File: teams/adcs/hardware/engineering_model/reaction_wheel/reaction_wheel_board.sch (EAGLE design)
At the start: 93 parts, among them U2 TPS732XX, U3 TPS732XX

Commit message: ADCS/RW: Include new SEPIC layout
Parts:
- added C8: 10 uF, rcl:C-USC0805
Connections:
- net N$1 renamed VD
- net GND: now also C8.2, U$2.WHEEL_GND@71, U$2.WHEEL_GND@72; no longer U$2.BDOT_3.3V@84, U$2.BDOT_5V@82
- net VBAT: now also C8.1, U$2.WHEEL_VBATT@69, U$2.WHEEL_VBATT@70; no longer U$2.BDOT_3.3V@83, U$2.BDOT_5V@81
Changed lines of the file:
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@@
 <?xml version="1.0" encoding="utf-8"?>
 <!DOCTYPE eagle SYSTEM "eagle.dtd">
-<eagle version="8.4.1">
+<eagle version="8.4.3">
 <drawing>
 <settings>
@@
 <part name="MOTOR_Y_DEBUG" library="SparkFun-Connectors" deviceset="CONN_03" device="LOCK"/>
 <part name="MOTOR_Z_DEBUG" library="SparkFun-Connectors" deviceset="CONN_03" device="LOCK"/>
+<part name="GND56" library="supply1" library_urn="urn:adsk.eagle:library:371" deviceset="GND" device=""/>
+<part name="C8" library="rcl" library_urn="urn:adsk.eagle:library:334" deviceset="C-US" device="C0805" package3d_urn="urn:adsk.eagle:package:23617/2" value="10 uF"/>
 </parts>
 <sheets>
@@
 <instance part="U$3" gate="G$1" x="0" y="-78.74"/>
 <instance part="U$4" gate="G$1" x="63.5" y="-129.54" rot="R270"/>
-<instance part="GND1" gate="1" x="20.32" y="25.4" rot="R90"/>
-<instance part="GND2" gate="1" x="96.52" y="25.4" rot="R90"/>
+<instance part="GND1" gate="1" x="33.02" y="33.02" rot="R270"/>
+<instance part="GND2" gate="1" x="93.98" y="33.02" rot="R90"/>
 <instance part="GND3" gate="1" x="71.12" y="-104.14" rot="R180"/>
 <instance part="GND4" gate="1" x="-48.26" y="-60.96" rot="R270"/>
@@
 <instance part="MOTOR_Y_DEBUG" gate="J$1" x="228.6" y="-58.42" rot="R180"/>
 <instance part="MOTOR_Z_DEBUG" gate="J$1" x="381" y="-58.42" rot="R180"/>
+<instance part="GND56" gate="1" x="-78.74" y="22.86"/>
+<instance part="C8" gate="G$1" x="-78.74" y="33.02"/>
 </instances>
 <busses>
@@
 <net name="GND" class="0">
 <segment>
-<pinref part="U$2" gate="G$1" pin="BDOT_5V@82"/>
-<pinref part="GND1" gate="1" pin="GND"/>
-<wire x1="12.7" y1="25.4" x2="17.78" y2="25.4" width="0.1524" layer="91"/>
-</segment>
-<segment>
-<pinref part="GND2" gate="1" pin="GND"/>
-<pinref part="U$2" gate="G$1" pin="BDOT_3.3V@84"/>
-<wire x1="93.98" y1="25.4" x2="88.9" y2="25.4" width="0.1524" layer="91"/>
-</segment>
-<segment>
 <pinref part="U$4" gate="G$1" pin="GND@2"/>
 <pinref part="GND3" gate="1" pin="GND"/>
@@
 <label x="368.3" y="-53.34" size="1.778" layer="95" rot="R180" xref="yes"/>
 </segment>
+<segment>
+<pinref part="U$2" gate="G$1" pin="WHEEL_GND@71"/>
+<pinref part="GND1" gate="1" pin="GND"/>
+<wire x1="35.56" y1="33.02" x2="38.1" y2="33.02" width="0.1524" layer="91"/>
+</segment>
+<segment>
+<pinref part="U$2" gate="G$1" pin="WHEEL_GND@72"/>
+<pinref part="GND2" gate="1" pin="GND"/>
+<wire x1="91.44" y1="33.02" x2="88.9" y2="33.02" width="0.1524" layer="91"/>
+</segment>
+<segment>
+<pinref part="GND56" gate="1" pin="GND"/>
+<pinref part="C8" gate="G$1" pin="2"/>
+<wire x1="-78.74" y1="25.4" x2="-78.74" y2="27.94" width="0.1524" layer="91"/>
+</segment>
 </net>
 <net name="CANH" class="0">
@@
 <net name="VBAT" class="0">
 <segment>
-<pinref part="U$2" gate="G$1" pin="BDOT_5V@81"/>
-<wire x1="-40.64" y1="25.4" x2="-45.72" y2="25.4" width="0.1524" layer="91"/>
-<label x="-45.72" y="25.4" size="1.778" layer="95" rot="R180" xref="yes"/>
-</segment>
-<segment>
-<pinref part="U$2" gate="G$1" pin="BDOT_3.3V@83"/>
-<wire x1="38.1" y1="25.4" x2="33.02" y2="25.4" width="0.1524" layer="91"/>
-<label x="33.02" y="25.4" size="1.778" layer="95" rot="R180" xref="yes"/>
+<label x="-50.8" y="30.48" size="1.778" layer="95" rot="R180" xref="yes"/>
+<wire x1="-45.72" y1="30.48" x2="-50.8" y2="30.48" width="0.1524" layer="91"/>
+<wire x1="-45.72" y1="30.48" x2="-45.72" y2="33.02" width="0.1524" layer="91"/>
+<pinref part="U$2" gate="G$1" pin="WHEEL_VBATT@69"/>
+<wire x1="-45.72" y1="33.02" x2="-40.64" y2="33.02" width="0.1524" layer="91"/>
 </segment>
 <segment>
@@
 <wire x1="187.96" y1="25.4" x2="187.96" y2="30.48" width="0.1524" layer="91"/>
 <junction x="187.96" y="25.4"/>
+</segment>
+<segment>
+<pinref part="U$2" gate="G$1" pin="WHEEL_VBATT@70"/>
+<wire x1="12.7" y1="33.02" x2="17.78" y2="33.02" width="0.1524" layer="91"/>
+<label x="17.78" y="33.02" size="1.778" layer="95" xref="yes"/>
+</segment>
+<segment>
+<pinref part="C8" gate="G$1" pin="1"/>
+<wire x1="-78.74" y1="35.56" x2="-78.74" y2="38.1" width="0.1524" layer="91"/>
+<label x="-78.74" y="38.1" size="1.778" layer="95" rot="R90" xref="yes"/>
 </segment>
 </net>
@@
 </segment>
 </net>
-<net name="N$1" class="0">
+<net name="VD" class="0">
 <segment>
 <pinref part="C25" gate="G$1" pin="2"/>

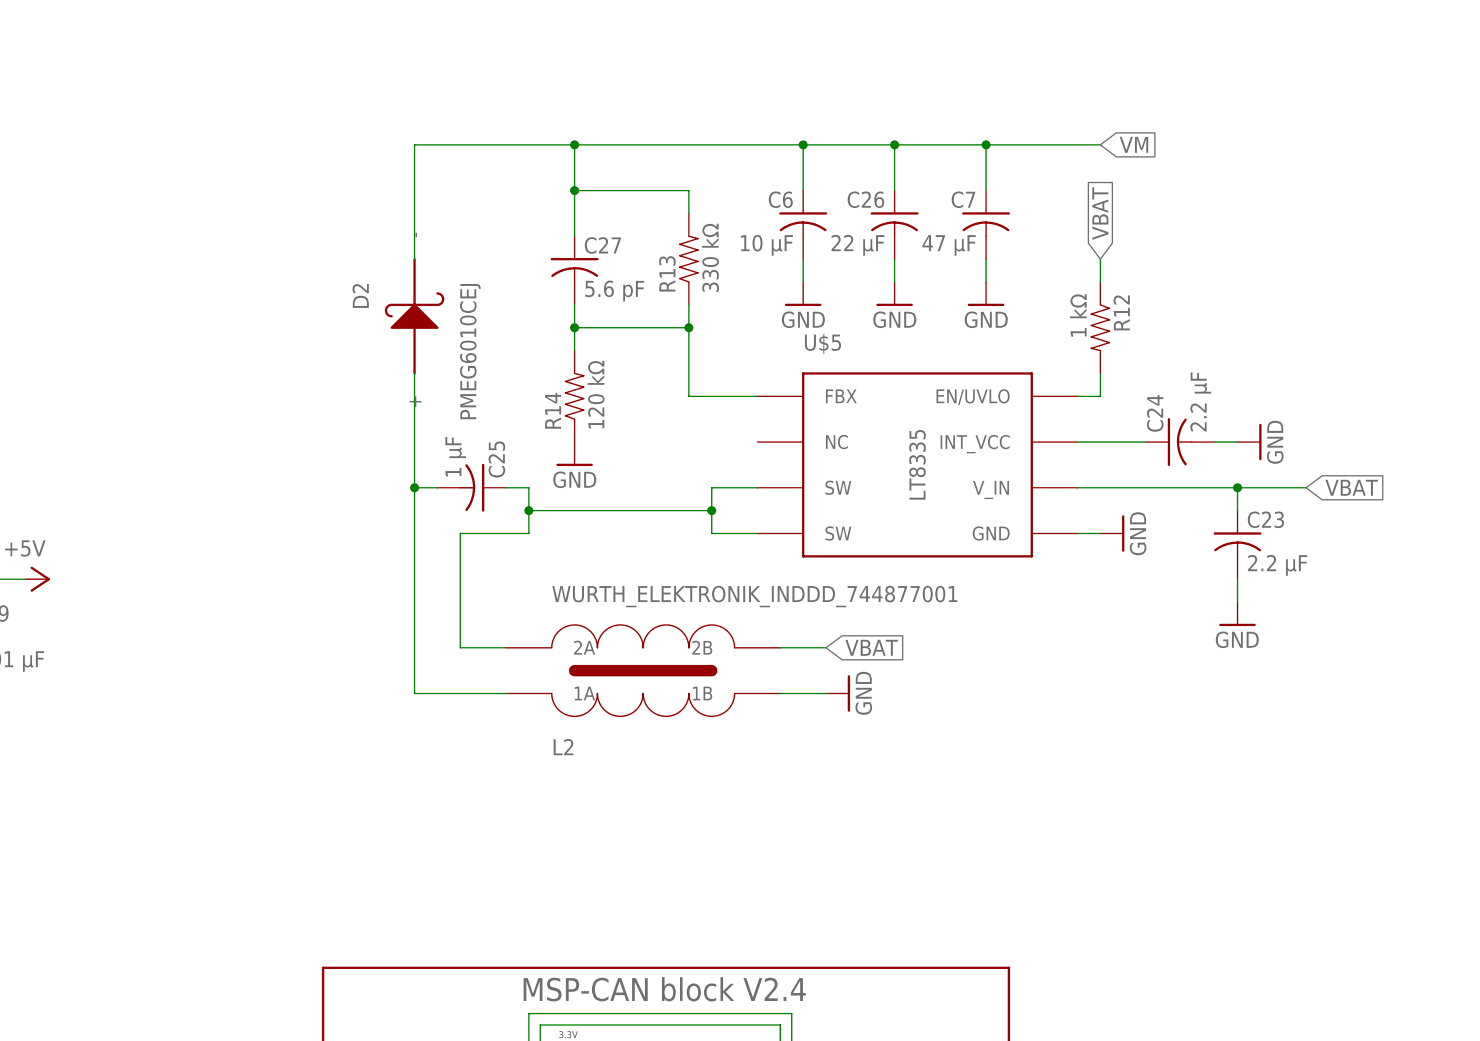
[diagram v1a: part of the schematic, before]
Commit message: ADCS: Switch to new SEPIC layout
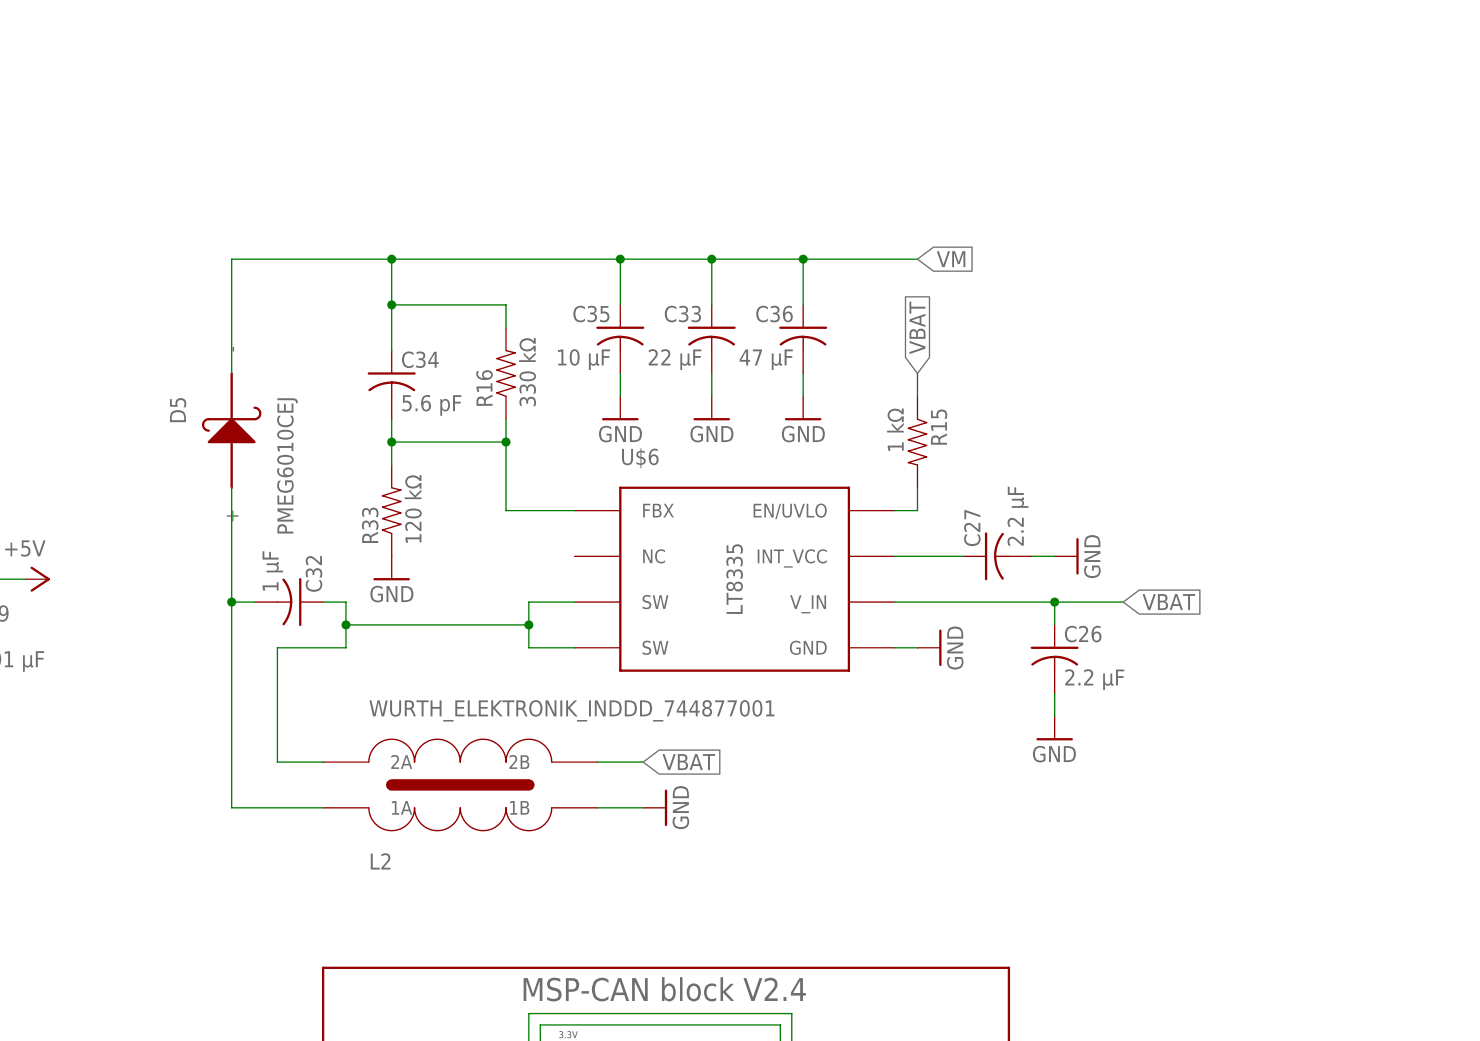
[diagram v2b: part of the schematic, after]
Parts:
- removed C23, C24: 2.2 μF, rcl:C-USC0805
- removed C25: 1 μF, rcl:C-USC0805
- removed C6: 10 μF, rcl:C-USC0805
- removed C7: 47 μF, rcl:C-USC1206
- removed D2: PMEG6010CEJ, DubSat1 Components:PMEG6010CEJ
- removed R12: 1 kΩ, DubSat1 Components:RESISTOR0805
- removed R13: 330 kΩ, DubSat1 Components:RESISTOR0805
- removed R14: 120 kΩ, DubSat1 Components:RESISTOR0805
- removed U$5: LT8335, DubSat1 Components:LT8335
- added C32: 1 μF, rcl:C-USC0805
- added C33: 22 μF, rcl:C-USC1206
- added C34: 5.6 pF, rcl:C-USC0805
- added C35: 10 μF, rcl:C-USC0805
- added C36: 47 μF, rcl:C-USC1206
- added D5: PMEG6010CEJ, DubSat1 Components:PMEG6010CEJ
- added R15: 1 kΩ, DubSat1 Components:RESISTOR0805
- added R16: 330 kΩ, DubSat1 Components:RESISTOR0805
- added R33: 120 kΩ, DubSat1 Components:RESISTOR0805
- added U$6: LT8335, DubSat1 Components:LT8335
- C26: value 22 μF -> 2.2 μF; device rcl:C-USC1206 -> rcl:C-USC0805
- C27: value 5.6 pF -> 2.2 μF
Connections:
- net EN_UVLO: now also R15.2, U$6.EN/UVLO; no longer R12.2, U$5.EN/UVLO
- net FBX: now also C34.2, R16.1, R33.2, U$6.FBX; no longer C27.2, R13.1, R14.2, U$5.FBX
- net GND: now also C27.2, C33.2, C35.2, C36.2, R33.1, U$6.GND; no longer C23.2, C24.2, C6.2, C7.2, R14.1, U$5.GND
- net INT_VCC: now also C27.1, U$6.INT_VCC; no longer C24.1, U$5.INT_VCC
- net SW: now also C32.1, U$6.SW@1, U$6.SW@2; no longer C25.1, U$5.SW@1, U$5.SW@2
- net VBAT: now also C26.1, R15.1, U$6.V_IN; no longer C23.1, R12.1, U$5.V_IN
- net VD: now also C32.2, D5.+; no longer C25.2, D2.+
- net VM: now also C33.1, C34.1, C35.1, C36.1, D5.-, R16.2; no longer C26.1, C27.1, C6.1, C7.1, D2.-, R13.2
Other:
- moved on the sheet: C26, C27, L2

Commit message: ADCS/RW: Update some net and component names
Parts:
- renumbered U$11 to MSP_Y_DEBUG, U$14 to MSP_Z_DEBUG, U$2 to PC104, U$4 to MSP_X_DEBUG

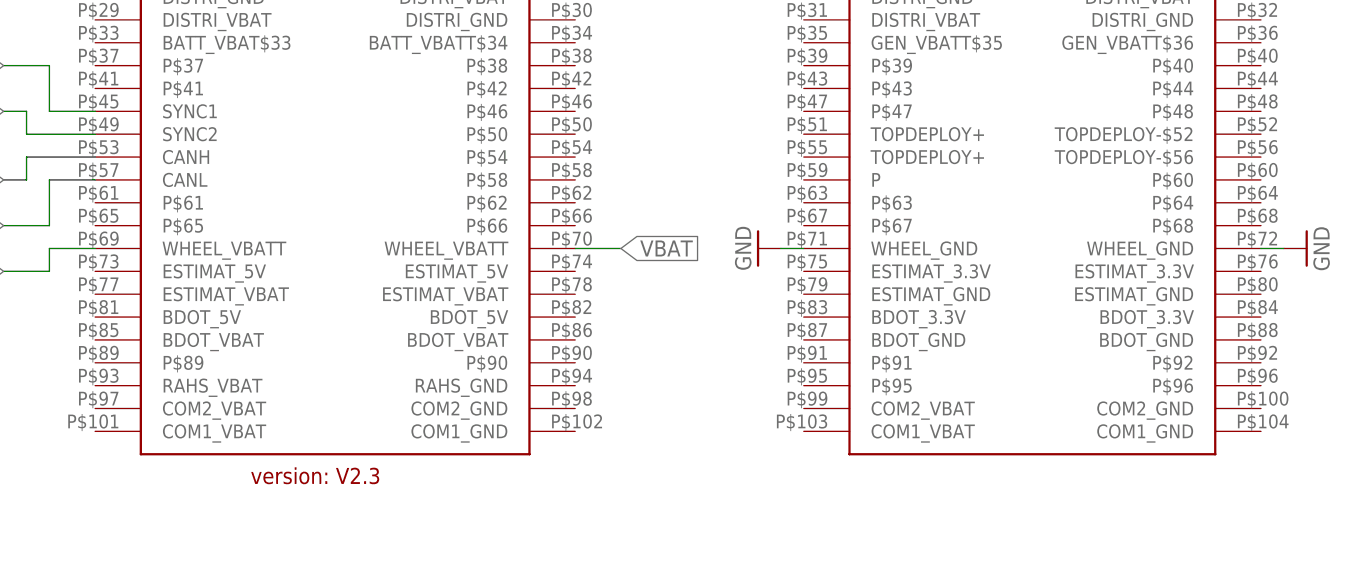
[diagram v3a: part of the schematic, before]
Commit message: ADCS/RW: Move debug LED out from under Picolock connector 😞
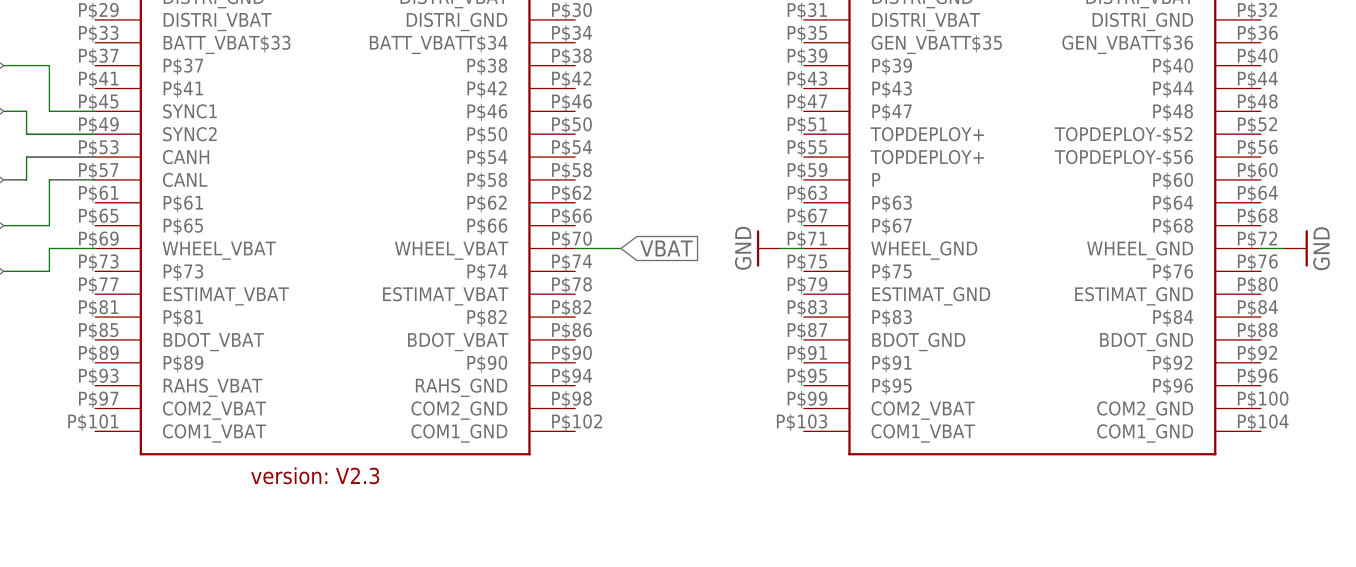
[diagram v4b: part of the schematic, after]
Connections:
- net VBAT: now also PC104.WHEEL_VBAT@69, PC104.WHEEL_VBAT@70; no longer PC104.WHEEL_VBATT@69, PC104.WHEEL_VBATT@70
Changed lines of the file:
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@@
 <?xml version="1.0" encoding="utf-8"?>
 <!DOCTYPE eagle SYSTEM "eagle.dtd">
-<eagle version="8.5.1">
+<eagle version="8.5.0">
 <drawing>
 <settings>
@@
 <wire x1="-45.72" y1="30.48" x2="-50.8" y2="30.48" width="0.1524" layer="91"/>
 <wire x1="-45.72" y1="30.48" x2="-45.72" y2="33.02" width="0.1524" layer="91"/>
-<pinref part="PC104" gate="G$1" pin="WHEEL_VBATT@69"/>
+<pinref part="PC104" gate="G$1" pin="WHEEL_VBAT@69"/>
 <wire x1="-45.72" y1="33.02" x2="-40.64" y2="33.02" width="0.1524" layer="91"/>
 </segment>
@@
 </segment>
 <segment>
-<pinref part="PC104" gate="G$1" pin="WHEEL_VBATT@70"/>
+<pinref part="PC104" gate="G$1" pin="WHEEL_VBAT@70"/>
 <wire x1="12.7" y1="33.02" x2="17.78" y2="33.02" width="0.1524" layer="91"/>
 <label x="17.78" y="33.02" size="1.778" layer="95" xref="yes"/>
@@
 packages will not be understood (or retained) with this version.
 </note>
+<note version="8.4" severity="warning">
+Since Version 8.4, EAGLE supports properties for SPICE simulation.
+Probes in schematics and SPICE mapping objects found in parts and library devices
+will not be understood with this version. Update EAGLE to the latest version
+for full support of SPICE simulation.
+</note>
 </compatibility>
